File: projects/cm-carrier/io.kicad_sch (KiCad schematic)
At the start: 16 parts, among them J8 micro HDMI (Type D), J9 microSD, U10 TPD4EUSB30, U11 TPD4EUSB30, U12 MagJack A70-112-331N126, U13 TPD4EUSB30, U14 TPD4EUSB30, U15 TPD4EUSB30, U16 RT9742SNGV, U17 RT9742GGJ5

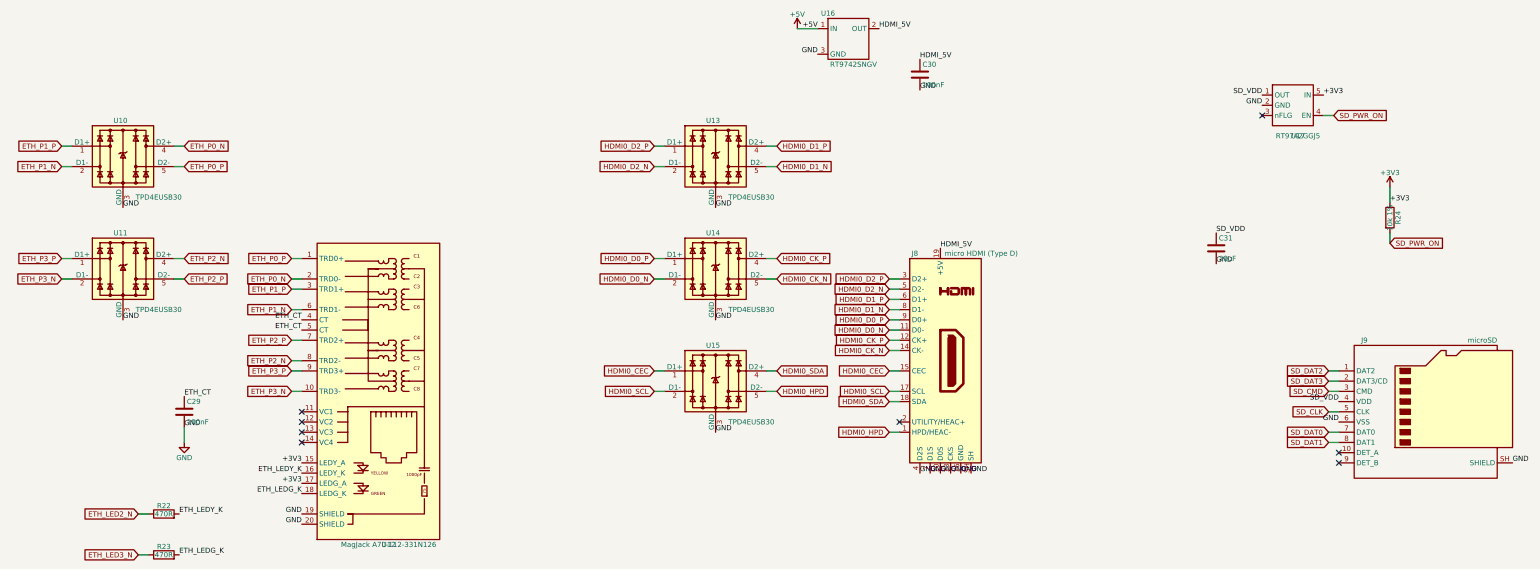
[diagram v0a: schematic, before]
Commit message: cm-carrier: schematic readability cleanup (no netlist change)
Co-Authored-By: Claude Opus 5.5 <noreply@anthropic.com>
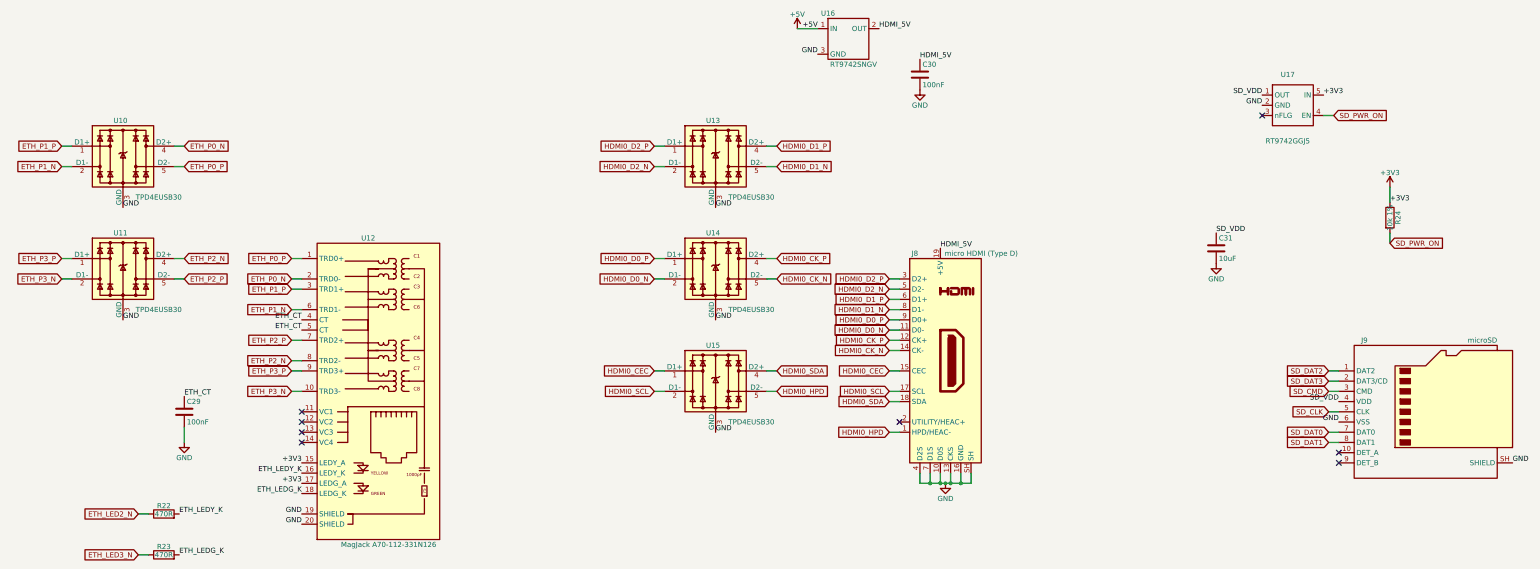
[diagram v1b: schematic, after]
